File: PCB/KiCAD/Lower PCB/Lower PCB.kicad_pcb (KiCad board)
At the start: 2 copper layers, 188.6 x 165.4 mm, 106 parts, among them IC1 ADG608BRZ, IC2 ADG608BRZ, IC3 ADG608BRZ, J1 Conn_01x02_MountingPin, J2 Conn_01x04_MountingPin, J3 Conn_01x04_MountingPin, J4 Conn_01x04_MountingPin, Q1 SFH320, Q10 SFH320, Q11 SFH320, Q12 SFH320, Q13 SFH320, Q14 SFH320, Q15 SFH320, Q16 SFH320, Q17 SFH320, Q18 SFH320, Q19 SFH320, Q2 SFH320, Q20 SFH320, Q21 SFH320, Q22 SFH320, Q23 SFH320, Q24 SFH320, Q3 SFH320, Q4 SFH320, Q5 SFH320, Q6 SFH320, Q7 SFH320, Q8 SFH320, Q9 SFH320

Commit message: Uh oh there was a +5V rail
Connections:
- Q1 pad 1: +5V -> +3V3
- Q10 pad 1: +5V -> +3V3
- Q11 pad 1: +5V -> +3V3
- Q12 pad 1: +5V -> +3V3
- Q13 pad 1: +5V -> +3V3
- Q14 pad 1: +5V -> +3V3
- Q15 pad 1: +5V -> +3V3
- Q16 pad 1: +5V -> +3V3
- Q17 pad 1: +5V -> +3V3
- Q18 pad 1: +5V -> +3V3
- Q19 pad 1: +5V -> +3V3
- Q2 pad 1: +5V -> +3V3
- Q20 pad 1: +5V -> +3V3
- Q21 pad 1: +5V -> +3V3
- Q22 pad 1: +5V -> +3V3
- Q23 pad 1: +5V -> +3V3
- Q24 pad 1: +5V -> +3V3
- Q3 pad 1: +5V -> +3V3
- Q4 pad 1: +5V -> +3V3
- Q5 pad 1: +5V -> +3V3
- Q6 pad 1: +5V -> +3V3
- Q7 pad 1: +5V -> +3V3
- Q8 pad 1: +5V -> +3V3
- Q9 pad 1: +5V -> +3V3
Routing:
- net GND: track 702.4 -> 0.00 mm, vias 19 -> 0
- net +5V: track 587.0 -> 0.00 mm, vias 15 -> 0
- net +3V3: track 535.4 -> 0.00 mm, vias 6 -> 0
- net Net-(IC2-S8): track 297.9 -> 0.00 mm, vias 8 -> 0
- net Net-(IC2-S7): track 212.2 -> 0.00 mm, vias 7 -> 0
- net Net-(IC2-S6): track 183.7 -> 0.00 mm, vias 3 -> 0
- net Net-(IC1-S8): track 174.9 -> 0.00 mm, vias 7 -> 0
- net Net-(IC2-S5): track 159.1 -> 0.00 mm, vias 4 -> 0
- net Net-(IC1-S7): track 158.0 -> 0.00 mm, vias 4 -> 0
- net Net-(IC2-S4): track 145.6 -> 0.00 mm, vias 3 -> 0
- net Net-(IC2-S2): track 141.3 -> 0.00 mm, vias 6 -> 0
- net Net-(IC2-S3): track 138.1 -> 0.00 mm, vias 3 -> 0
- net Net-(IC1-S6): track 130.6 -> 0.00 mm, vias 9 -> 0
- net Net-(IC1-S5): track 130.3 -> 0.00 mm, vias 4 -> 0
- net Net-(IC1-S4): track 123.3 -> 0.00 mm, vias 4 -> 0
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
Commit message: Start of tracing again
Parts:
- moved R1 6.36 mm to (5.75, 57.0), turned to 90 degrees
- moved R13 6.02 mm to (1.25, -82.0), turned to -90 degrees
- moved R2 5.03 mm to (3.50, 57.0), turned to 90 degrees
- moved R52 4.75 mm to (19.5, 57.0), turned to -90 degrees
- moved R12 4.59 mm to (-1.25, -82.0), turned to -90 degrees
- moved R14 4.59 mm to (3.50, -82.0), turned to -90 degrees
- moved R17 4.59 mm to (81.2, -10.0), turned to 180 degrees
- moved R34 4.59 mm to (-77.2, 12.2), turned to 0 degrees
- moved R37 4.59 mm to (-77.2, -7.75), turned to 0 degrees
- moved R40 4.59 mm to (-5.75, -78.0), turned to -90 degrees
- moved R44 4.59 mm to (3.50, -78.0), turned to -90 degrees
- moved R47 4.59 mm to (77.2, -10.0), turned to 180 degrees
- moved R49 4.59 mm to (77.2, 7.75), turned to 180 degrees
- moved R6 4.59 mm to (-81.2, 7.75), turned to 0 degrees
- moved R9 4.59 mm to (-81.2, -12.2), turned to 0 degrees
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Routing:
- net +3V3: track 0.00 -> 673.0 mm, vias 0 -> 19
- net GND: track 0.00 -> 661.5 mm, vias 0 -> 25
- net Net-(IC2-S8): track 0.00 -> 294.9 mm, vias 0 -> 7
- net Net-(IC2-S7): track 0.00 -> 218.5 mm, vias 0 -> 3
- net Net-(IC2-S6): track 0.00 -> 179.5 mm, vias 0 -> 3
- net Net-(IC1-S8): track 0.00 -> 177.2 mm, vias 0 -> 6
- net Net-(IC2-S5): track 0.00 -> 152.3 mm, vias 0 -> 3
- net Net-(IC2-S4): track 0.00 -> 148.8 mm, vias 0 -> 3
- net Net-(IC1-S7): track 0.00 -> 148.3 mm, vias 0 -> 5
- net Net-(IC2-S3): track 0.00 -> 136.5 mm, vias 0 -> 4
- net Net-(IC2-S2): track 0.00 -> 133.1 mm, vias 0 -> 3
- net Net-(IC1-S6): track 0.00 -> 130.9 mm, vias 0 -> 6
- net Net-(IC3-S8): track 0.00 -> 129.4 mm, vias 0 -> 2
- net Net-(IC1-S5): track 0.00 -> 121.3 mm, vias 0 -> 4
- net Net-(IC1-S4): track 0.00 -> 118.6 mm, vias 0 -> 2
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
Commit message: More trace optimizations
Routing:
- net Net-(IC3-S5): track 79.8 -> 129.1 mm, vias 3 -> 2
- net Net-(IC2-S3): track 136.5 -> 157.8 mm, vias 4 -> 5
- net Net-(IC1-S8): track 177.2 -> 159.7 mm, vias 6 -> 2
- net GND: track 661.5 -> 678.8 mm
- net Net-(IC1-S4): track 118.6 -> 132.3 mm, vias 2 -> 1
- net Net-(IC2-S8): track 294.9 -> 282.5 mm, vias 7 -> 5
- net Net-(D10-A): track 61.0 -> 53.2 mm
- net Net-(D22-A): track 40.4 -> 33.6 mm
- net Net-(IC1-S6): track 130.9 -> 124.3 mm, vias 6 -> 2
- net Net-(IC1-S7): track 148.3 -> 143.1 mm, vias 5 -> 3
- net Net-(D3-A): track 50.4 -> 45.6 mm, vias 3 -> 1
- net Net-(IC3-S6): track 107.2 -> 102.4 mm
- net Net-(D21-A): track 46.2 -> 41.5 mm
- net Net-(IC3-S3): track 32.9 -> 28.3 mm
- net Net-(D5-A): track 32.2 -> 28.1 mm
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
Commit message: More tweaks
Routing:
- net Net-(IC2-S8): track 282.5 -> 245.0 mm, vias 5 -> 2
- net GND: track 678.8 -> 646.3 mm, vias 25 -> 23
- net LED_1_A0: track 24.0 -> 43.8 mm, vias 4 -> 0
- net Net-(IC1-S4): track 132.3 -> 117.8 mm, vias 1 -> 2
- net LED_1_A1: track 21.4 -> 29.2 mm, vias 2 -> 0
- net Net-(IC3-S8): track 126.8 -> 119.9 mm, vias 2 -> 1
- net Net-(IC1-S8): track 159.7 -> 165.7 mm
- net Net-(D22-A): track 33.6 -> 27.9 mm
- net Net-(IC1-S2): track 51.9 -> 56.6 mm
- net Net-(IC1-S5): track 118.3 -> 113.8 mm, vias 3 -> 2
- net LED_1_A2: track 27.4 -> 30.9 mm
- net Net-(D23-A): track 13.0 -> 11.8 mm
- net LED_1_OUT: track 20.9 -> 19.9 mm
- net +3V3: track 670.6 -> 671.5 mm
- net Net-(IC1-S6): track 124.3 -> 123.6 mm, vias 2 -> 1
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
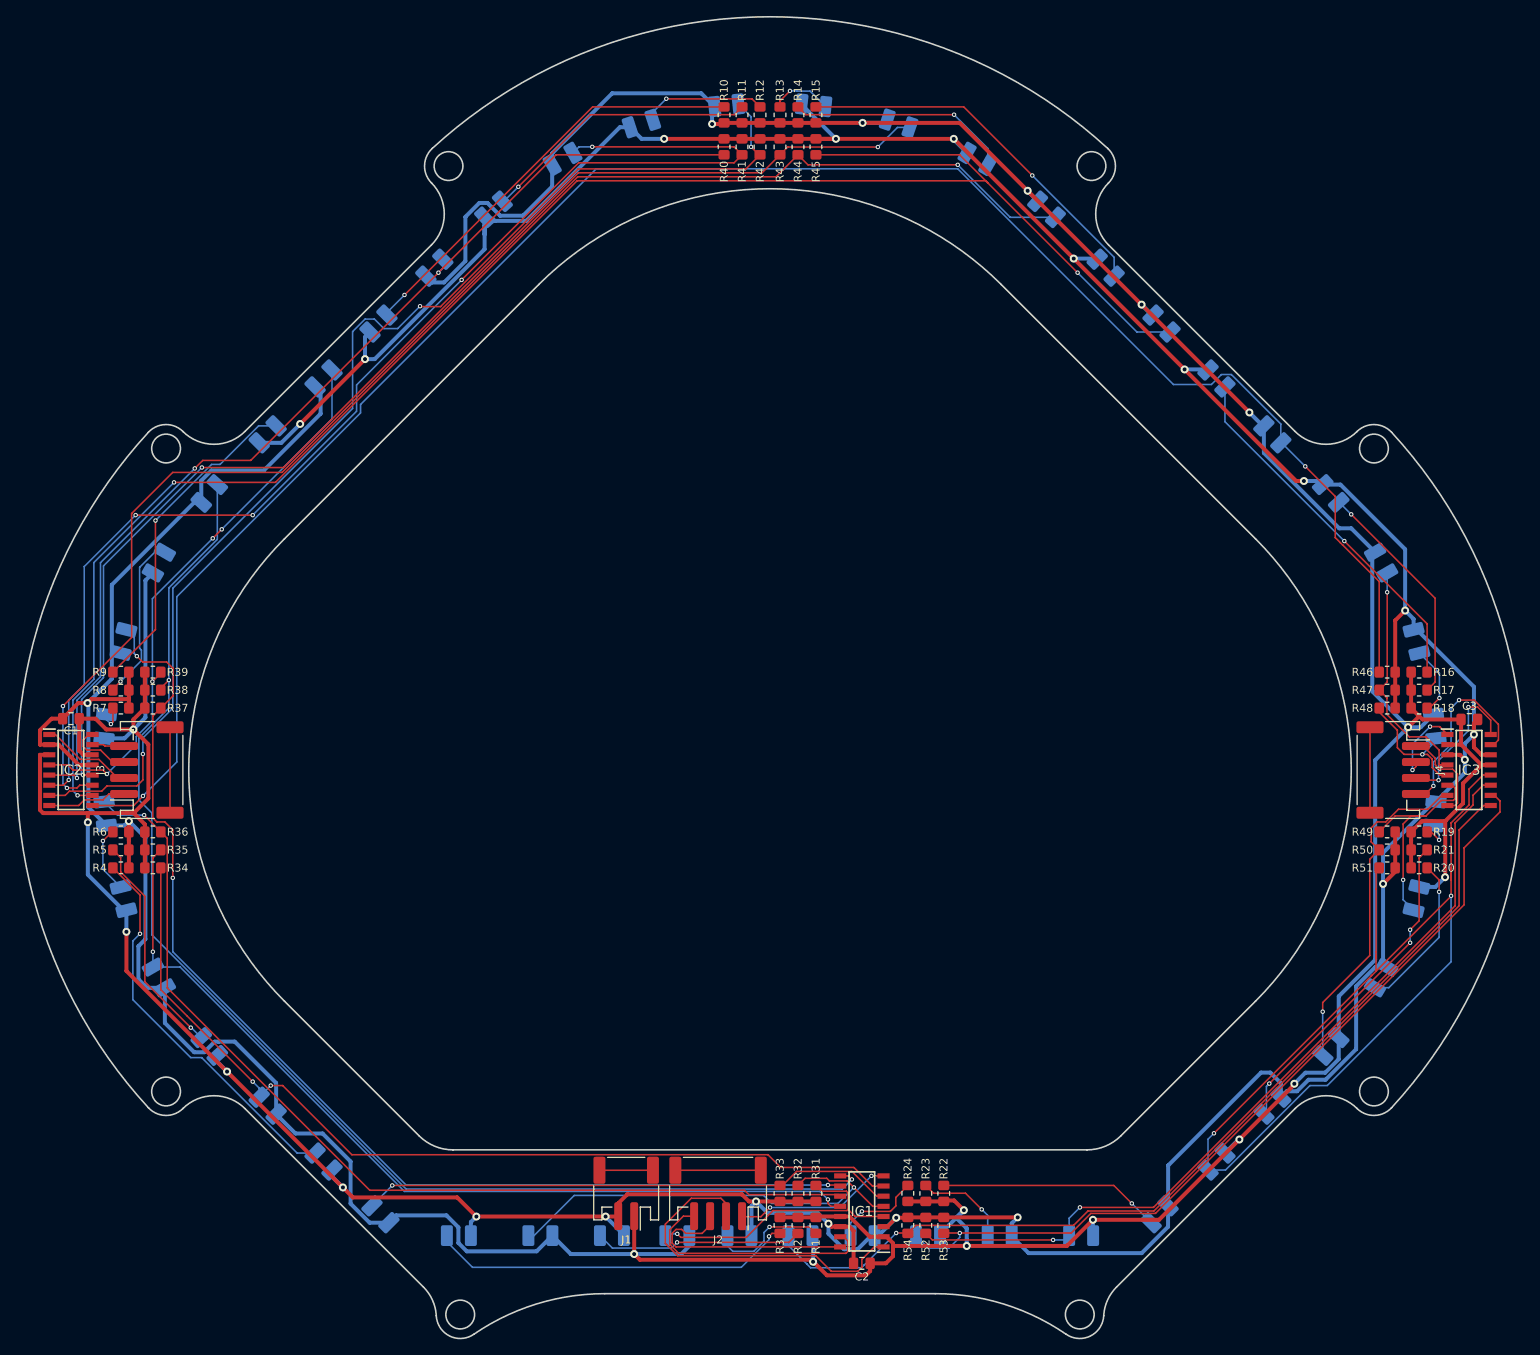
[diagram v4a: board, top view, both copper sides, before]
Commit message: More tweaks to the lower PCB
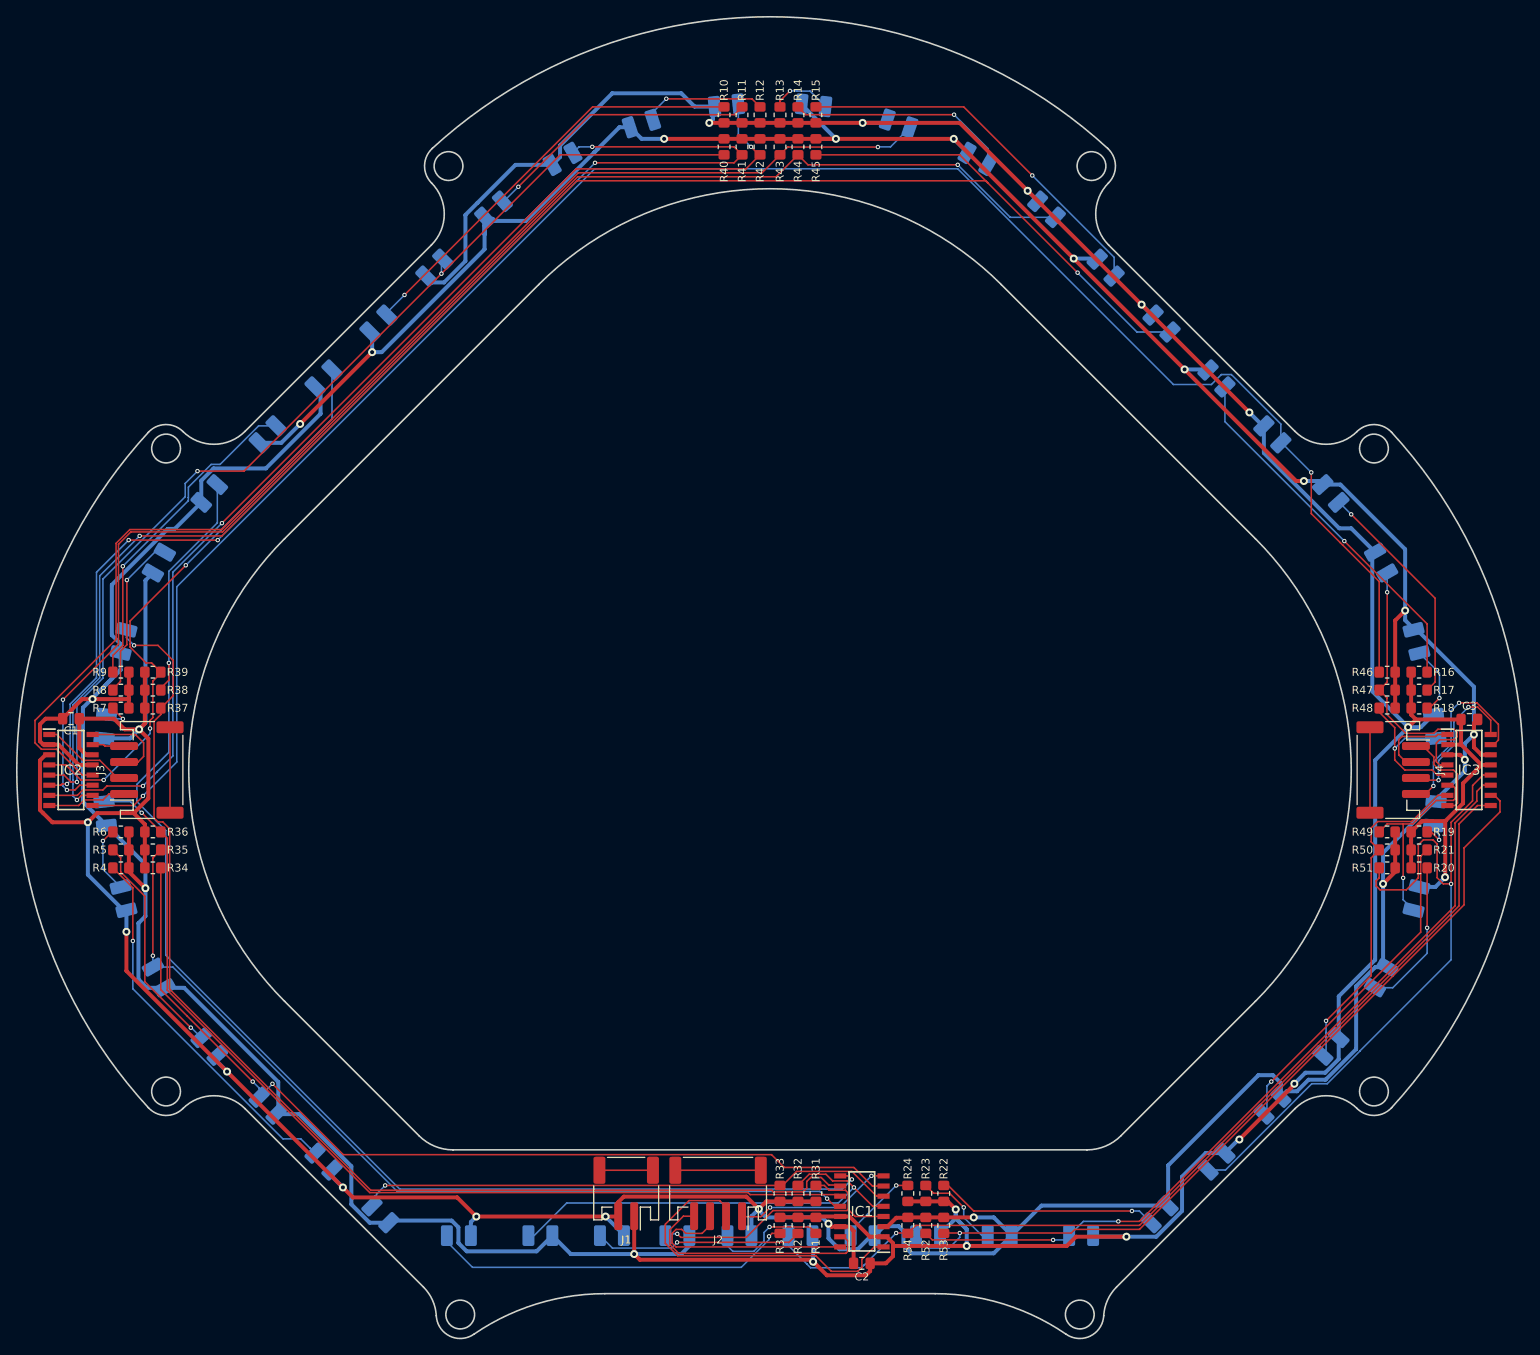
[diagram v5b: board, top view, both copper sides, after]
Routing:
- net Net-(IC3-S5): track 129.3 -> 88.8 mm, vias 2 -> 1
- net GND: track 646.3 -> 655.8 mm, vias 23 -> 22
- net Net-(IC2-S5): track 152.3 -> 159.0 mm, vias 3 -> 1
- net Net-(IC3-S1): track 29.8 -> 36.0 mm
- net Net-(IC2-S4): track 148.3 -> 143.2 mm
- net Net-(IC1-S7): track 142.8 -> 147.4 mm, vias 3 -> 1
- net +3V3: track 671.5 -> 667.6 mm
- net Net-(IC3-S2): track 16.9 -> 20.4 mm
- net Net-(IC3-S3): track 28.3 -> 25.0 mm
- net Net-(IC2-S3): track 157.7 -> 154.6 mm
- net LED_2_A1: track 8.17 -> 11.3 mm
- net Net-(IC1-S8): track 165.7 -> 168.5 mm
- net Net-(IC2-S1): track 71.5 -> 74.4 mm, vias 4 -> 3
- net Net-(D4-A): track 49.0 -> 47.5 mm
- net Net-(IC3-S6): track 102.7 -> 101.4 mm
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
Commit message: Added another switch
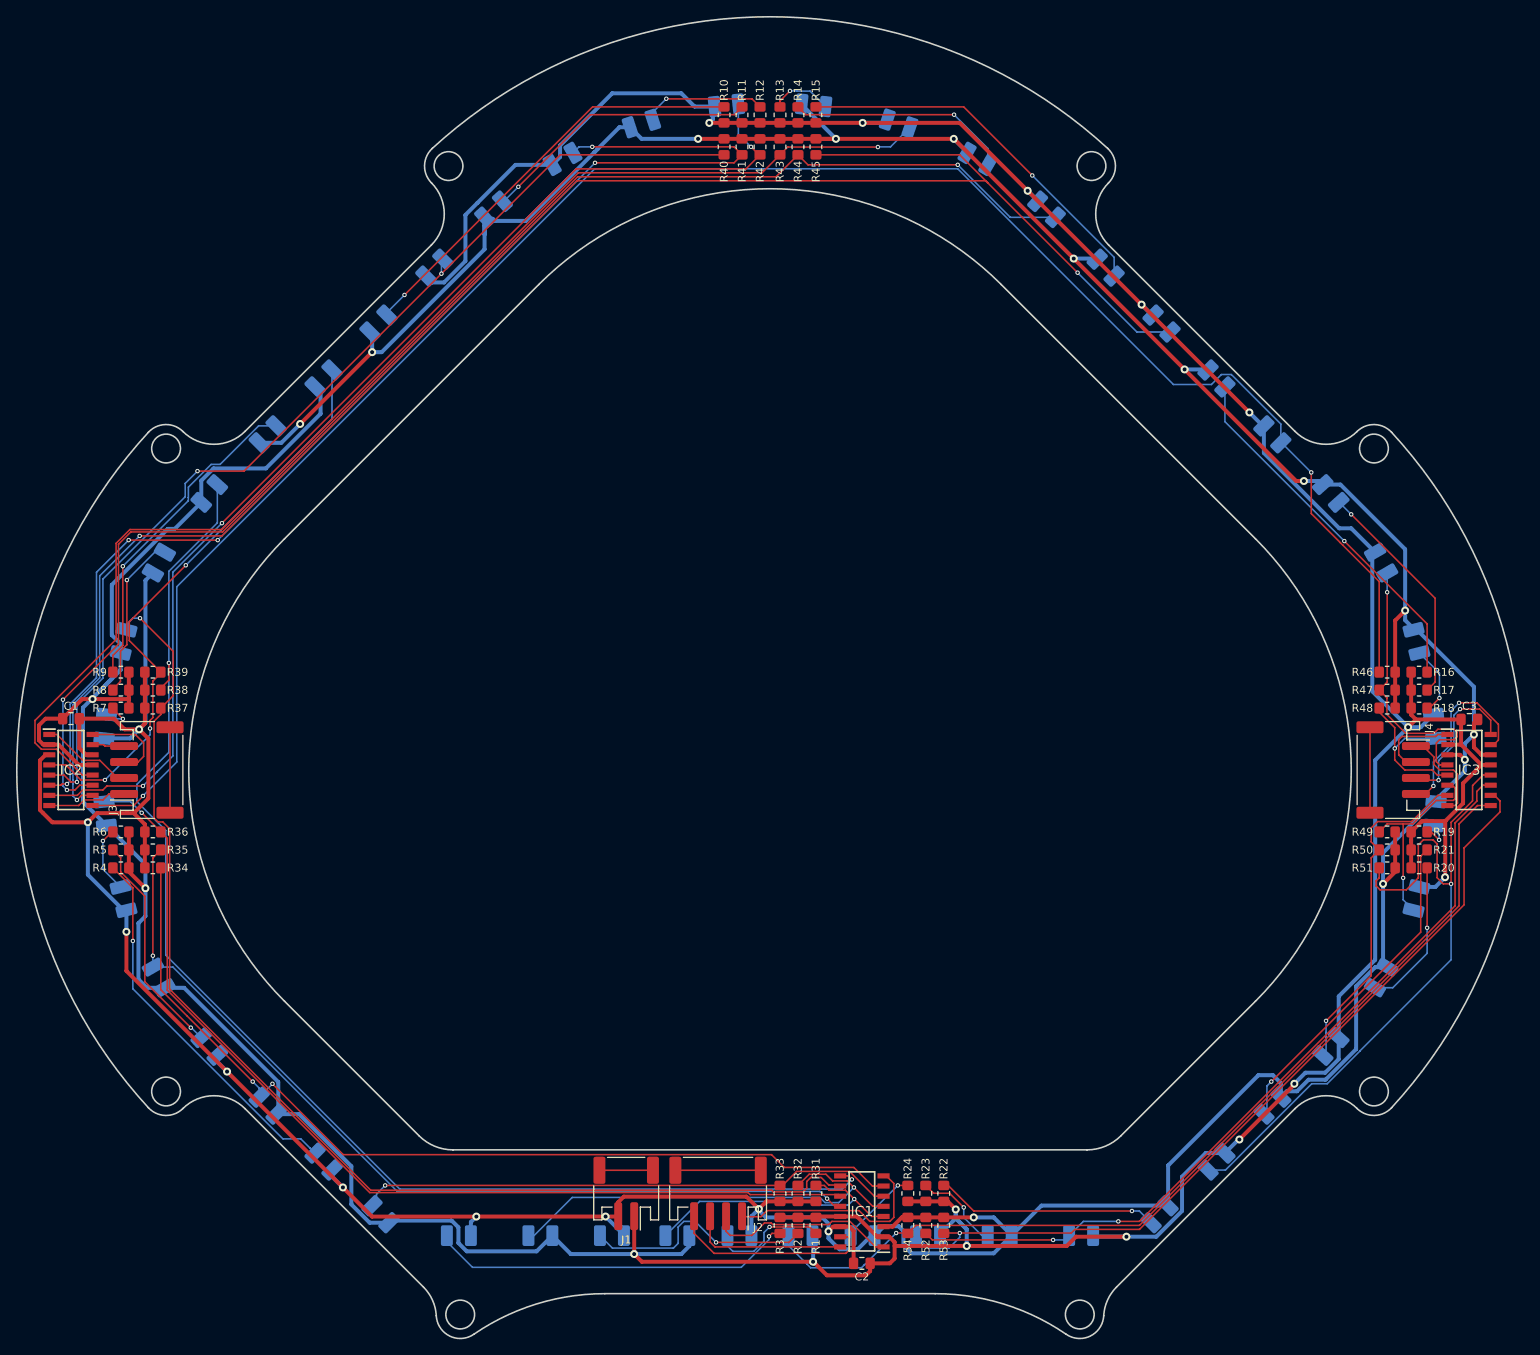
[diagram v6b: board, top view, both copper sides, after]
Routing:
- net LED_1_A0: track 43.3 -> 24.0 mm
- net LED_1_A1: track 29.2 -> 19.8 mm
- net LED_1_OUT: track 19.9 -> 26.0 mm, vias 2 -> 0
- net LED_1_A2: track 30.9 -> 25.5 mm
- net Net-(D2-A): track 26.2 -> 29.6 mm
- net Net-(IC1-S7): track 147.4 -> 149.1 mm
- net +3V3: track 667.6 -> 668.4 mm
- net Net-(IC1-S1): track 35.9 -> 36.5 mm
- net Net-(IC1-S2): track 56.2 -> 56.7 mm
